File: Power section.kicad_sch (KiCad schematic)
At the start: 15 parts, among them J2 USB3_A, U4 TLV76733, U5 USBLC6-2P6, U6 TPS7A0212

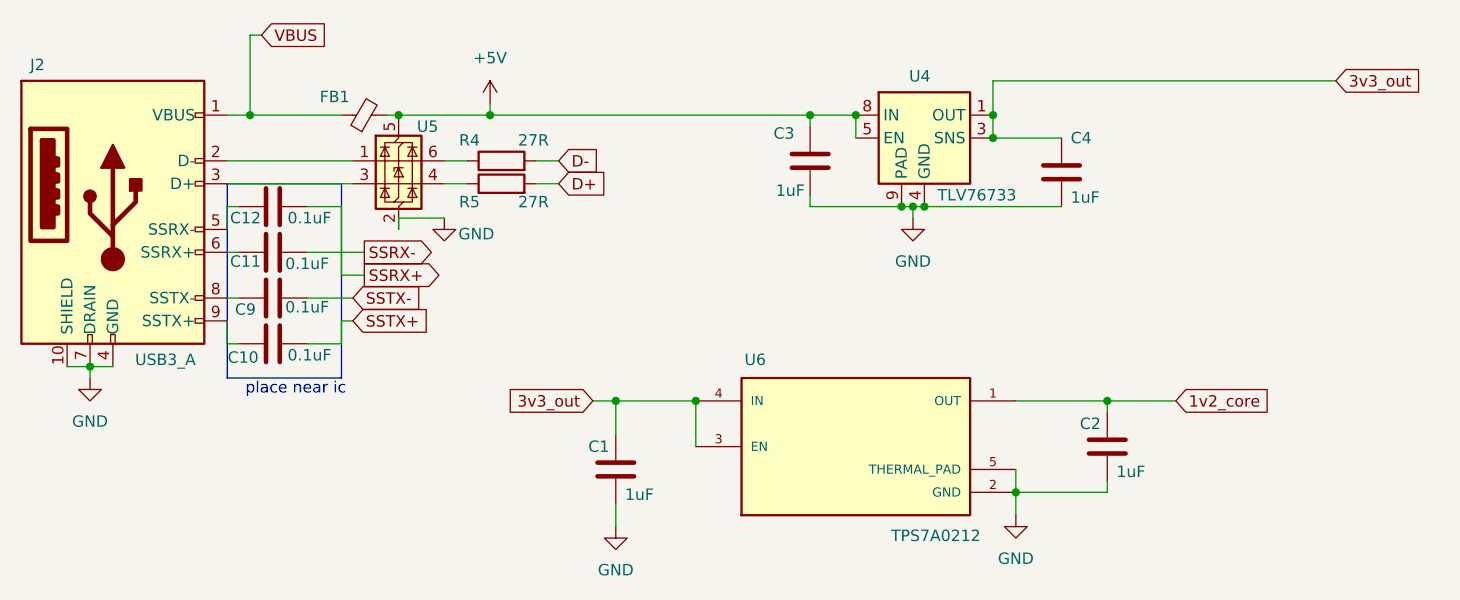
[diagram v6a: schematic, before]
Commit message: 1. Layout placement started. placed Lan7801, PHY, EEPROM and regulators 2.changed D+ D- lines of USB-TVS diode reveresed for clean routing
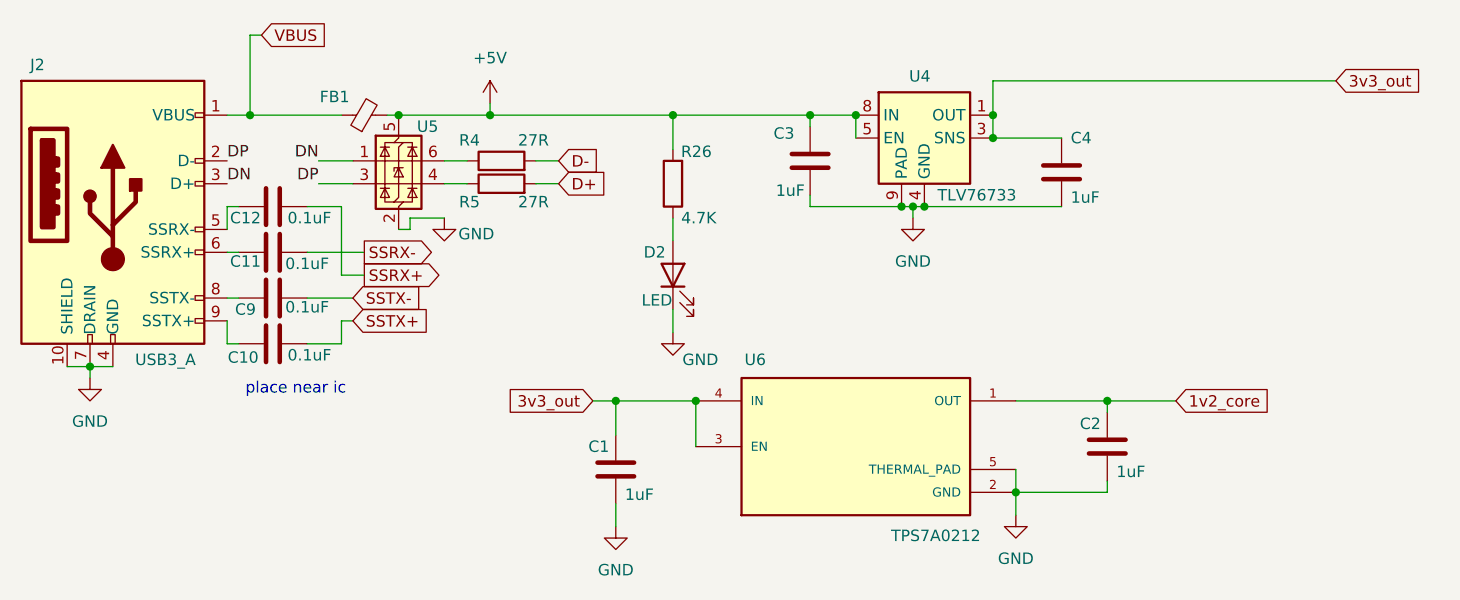
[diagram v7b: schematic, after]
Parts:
- added D2: LED, LED_SMD:LED_01005_0402Metric, symbol Device:LED
- added R26: 4.7K, Resistor_SMD:R_0402_1005Metric, symbol Device:R
- C1, C2, C3, C4: footprint Capacitor_SMD:C_0805_2012Metric -> Capacitor_SMD:C_0402_1005Metric
- C10, C11, C12, C9: footprint Capacitor_SMD:C_1206_3216Metric_Pad1.33x1.80mm_HandSolder -> Capacitor_SMD:C_0402_1005Metric
- FB1: footprint Inductor_SMD:L_0603_1608Metric_Pad1.05x0.95mm_HandSolder -> Inductor_SMD:L_0402_1005Metric
- R4, R5: footprint Resistor_SMD:R_1206 -> Resistor_SMD:R_0402_1005Metric
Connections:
- net +5V: now also R26.2
- net GND: now also D2.1 (K)
- net DN: now reaches U5.1 (I/O1)
- net DN: now also J2.3 (D+); no longer J2.2 (D-)
- net DP: now reaches U5.3 (I/O2)
- net DP: now also J2.2 (D-); no longer J2.3 (D+)
- new net: D2.2 (A), R26.1

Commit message: merged with main branch, no major change in pcb or schematics
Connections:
- net SSRX+: now also C11.2; no longer C12.2
- net SSRX-: now also C12.2; no longer C11.2
- net sstx_N: now reaches C9.1, J2.8 (SSTX-)
- net ssrx_N: now reaches C12.1, J2.5 (SSRX-)
- net ssrx_P: now reaches C11.1, J2.6 (SSRX+)
- net sstx_P: now reaches C10.1, J2.9 (SSTX+)
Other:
- moved on the sheet: C10, C11, C12, C9
